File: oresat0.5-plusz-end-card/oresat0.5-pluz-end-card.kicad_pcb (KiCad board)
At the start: 4 copper layers, 99.8 x 94.6 mm, 45 parts, among them J1 J-SAMTEC-TFM-120-01-L-D-RA, J2 Harwin M55-7101242R, J3 Harwin M55-7101242R, J4 Harwin M55-7101242R, J5 Harwin M55-7101242R, J6 Conn_Coaxial

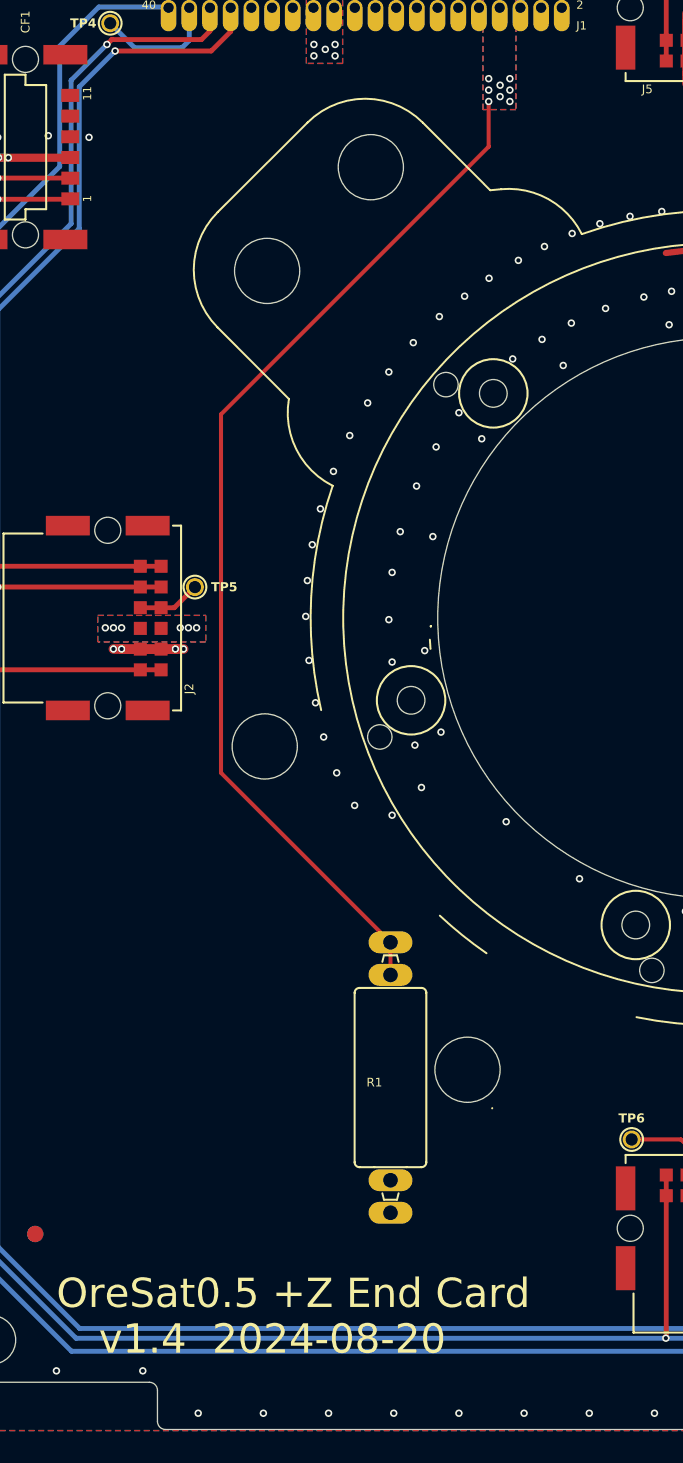
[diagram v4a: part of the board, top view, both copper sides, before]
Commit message: fixed silkscreen, fixed resistor helical deployer zone
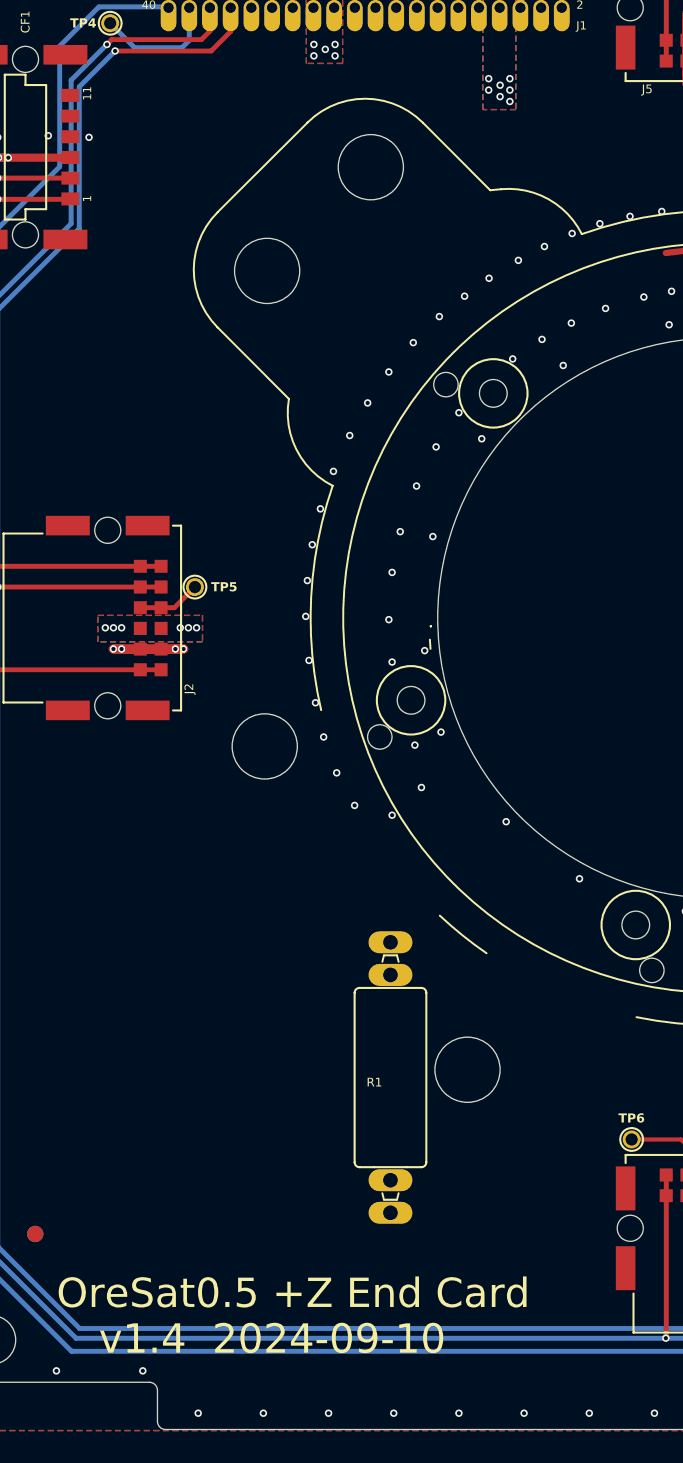
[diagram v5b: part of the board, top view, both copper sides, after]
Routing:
- net /HELICAL-DEPLOY: track 64.7 -> 0.00 mm, vias 8 -> 7
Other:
- board text added: "v1.4 2024-09-10"
- board text removed: "v1.4 2024-08-20"
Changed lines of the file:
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@@
 		(layer "F.SilkS")
 	)
-	(gr_line
-		(start 134.646944 132.575792)
-		(end 134.639949 132.592268)
-		(stroke
-			(width 0.12)
-			(type solid)
-		)
-		(layer "F.SilkS")
-	)
 	(gr_arc
 		(start 123.315615 72.08862)
@@
 		(layer "F.Fab")
 	)
-	(gr_text "v1.4  2024-08-20"
+	(gr_text "v1.4  2024-09-10"
 		(at 110.5 147.8 0)
 		(layer "F.SilkS")
@@
 		(net 4)
 	)
-	(segment
-		(start 118 90)
-		(end 134.4273 73.5727)
-		(width 0.25)
-		(layer "F.Cu")
-		(net 9)
-	)
-	(segment
-		(start 134.4273 73.5727)
-		(end 134.4273 70.8)
-		(width 0.25)
-		(layer "F.Cu")
-		(net 9)
-	)
-	(segment
-		(start 118 112)
-		(end 118 90)
-		(width 0.25)
-		(layer "F.Cu")
-		(net 9)
-	)
-	(segment
-		(start 128.400001 124.399999)
-		(end 128.400001 122.400001)
-		(width 0.25)
-		(layer "F.Cu")
-		(net 9)
-	)
-	(segment
-		(start 128.400001 122.400001)
-		(end 128.4 122.4)
-		(width 0.25)
-		(layer "F.Cu")
-		(net 9)
-	)
-	(segment
-		(start 128.4 122.4)
-		(end 118 112)
-		(width 0.25)
-		(layer "F.Cu")
-		(net 9)
-	)
 	(via
 		(at 135.7273 70.1)
@@
 		(net 9)
 	)
-	(via
-		(at 134.4273 70.8)
-		(size 0.4572)
-		(drill 0.254)
-		(layers "F.Cu" "B.Cu")
-		(free yes)
-		(net 9)
-	)
 	(segment
 		(start 120.8 59.9)
@@
 		(polygon
 			(pts
-				(xy 117.0635 103.9635) (xy 110.4365 103.9635) (xy 110.4365 102.3365) (xy 117.0635 102.3365)
+				(xy 116.8635 103.9635) (xy 110.4365 103.9635) (xy 110.4365 102.3365) (xy 116.8635 102.3365)
 			)
 		)
@@
 		(polygon
 			(pts
-				(xy 136.5 76.2) (xy 122 90.7) (xy 122 113.4) (xy 133.1 124.5) (xy 133.1 127.6) (xy 128.2 127.6)
-				(xy 128.2 124.596094) (xy 118 115) (xy 118 90) (xy 133.5 75) (xy 133.5 69.1) (xy 136.5 69.1)
+				(xy 136.5 76.2) (xy 122 90.7) (xy 122 108.4) (xy 120.140624 111.540624) (xy 130.6 122) (xy 130.6 126.1)
+				(xy 125.3 126.1) (xy 125.3 122.607522) (xy 113.515619 111.330111) (xy 117.6 106.086469) (xy 117.6 90.387096)
+				(xy 133.5 75) (xy 133.5 69.1) (xy 136.5 69.1)
 			)
 		)
@@
 			(pts
 				(xy 125.5635 65.8365) (xy 148.6635 65.8365) (xy 148.6635 68.4635) (xy 109.626302 68.4635) (xy 104.6635 73.426302)
-				(xy 104.6635 101.6365) (xy 117.0635 101.6365) (xy 117.0635 104.4635) (xy 104.6635 104.4635) (xy 104.6635 117.673698)
+				(xy 104.6635 101.6365) (xy 116.8635 101.6365) (xy 116.8635 104.4635) (xy 104.6635 104.4635) (xy 104.6635 117.673698)
 				(xy 130.326302 143.3365) (xy 147.5365 143.3365) (xy 147.5365 133.9365) (xy 150.6635 133.9365) (xy 150.6635 143.3365)
 				(xy 157.573585 143.3365) (xy 181.1365 119.800226) (xy 181.1365 101.0365) (xy 185.2635 101.0365)

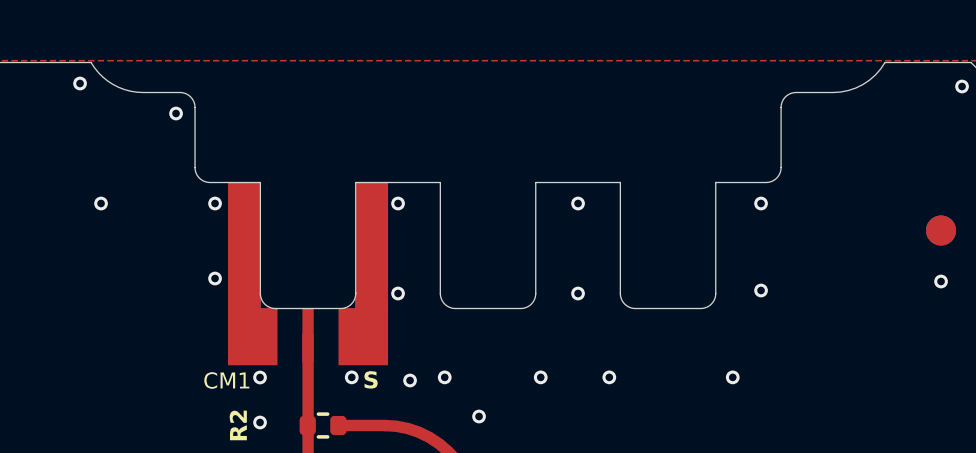
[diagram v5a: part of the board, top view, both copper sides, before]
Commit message: added components in symbol field for BOM
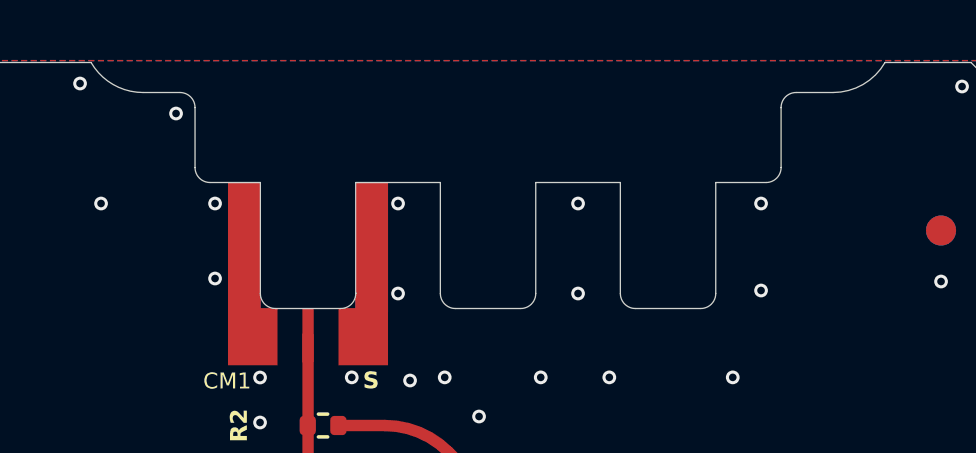
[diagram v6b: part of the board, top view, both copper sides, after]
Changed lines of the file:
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@@
 		(fp_arc
 			(start 17.73205 -43.8)
-			(mid 18.085606 -43.653542)
+			(mid 18.085571 -43.653536)
 			(end 18.23205 -43.3)
 			(stroke
@@
 		(fp_arc
 			(start 18.73205 -40.8)
-			(mid 18.378494 -40.946458)
+			(mid 18.378529 -40.946464)
 			(end 18.23205 -41.3)
 			(stroke
@@
 		(fp_arc
 			(start 37.76795 -43.3)
-			(mid 37.9144 -43.653536)
+			(mid 37.914394 -43.653571)
 			(end 38.26795 -43.8)
 			(stroke
@@
 		(fp_arc
 			(start 37.76795 -41.3)
-			(mid 37.6215 -40.946464)
+			(mid 37.621506 -40.946429)
 			(end 37.26795 -40.8)
 			(stroke
@@
 		(fp_arc
 			(start 17.73205 -43.8)
-			(mid 18.085606 -43.653542)
+			(mid 18.085571 -43.653536)
 			(end 18.23205 -43.3)
 			(stroke
@@
 		(fp_arc
 			(start 18.73205 -40.8)
-			(mid 18.378494 -40.946458)
+			(mid 18.378529 -40.946464)
 			(end 18.23205 -41.3)
 			(stroke
@@
 		(fp_arc
 			(start 37.76795 -43.3)
-			(mid 37.9144 -43.653536)
+			(mid 37.914394 -43.653571)
 			(end 38.26795 -43.8)
 			(stroke
@@
 		(fp_arc
 			(start 37.76795 -41.3)
-			(mid 37.6215 -40.946464)
+			(mid 37.621506 -40.946429)
 			(end 37.26795 -40.8)
 			(stroke

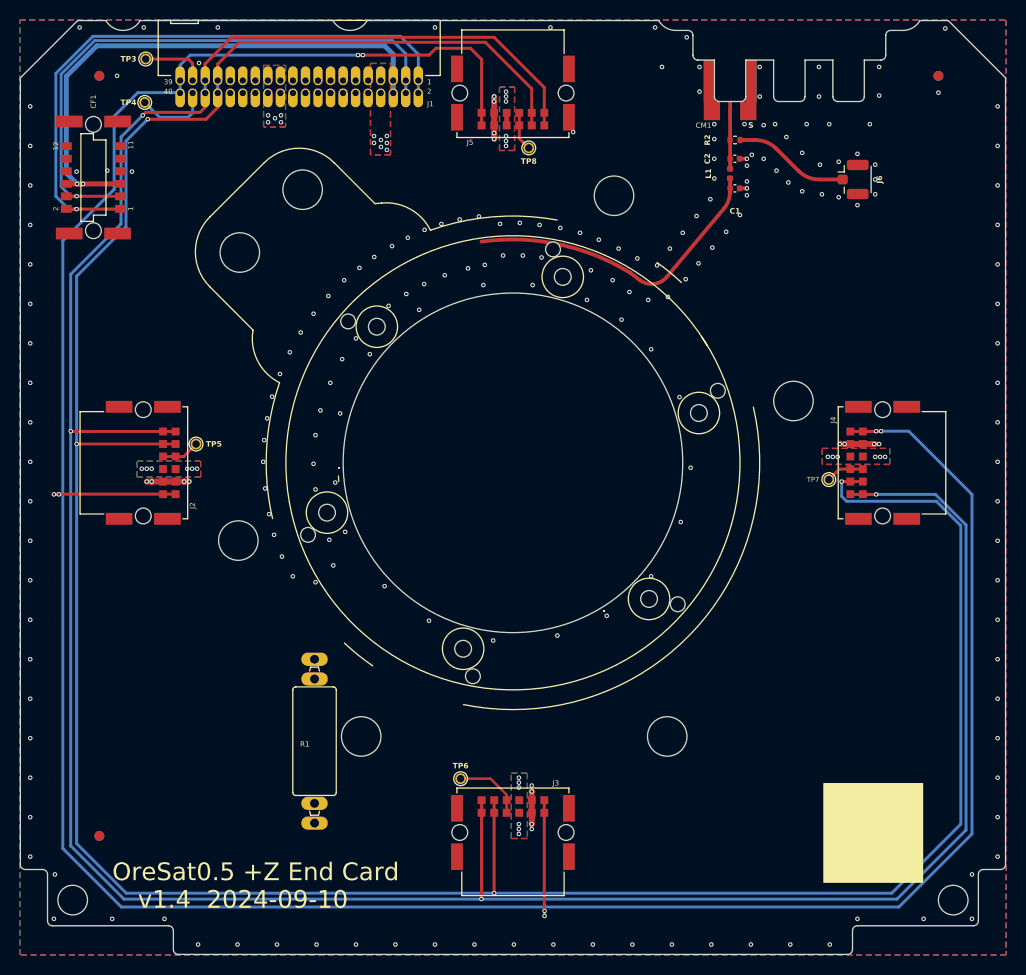
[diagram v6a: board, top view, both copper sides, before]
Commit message: Final polish for v1.4. Added more stiching vias, cleaned up some DRCs that were stupid, added more layers to deployment resistor pads, now  sending off to Osh Park.
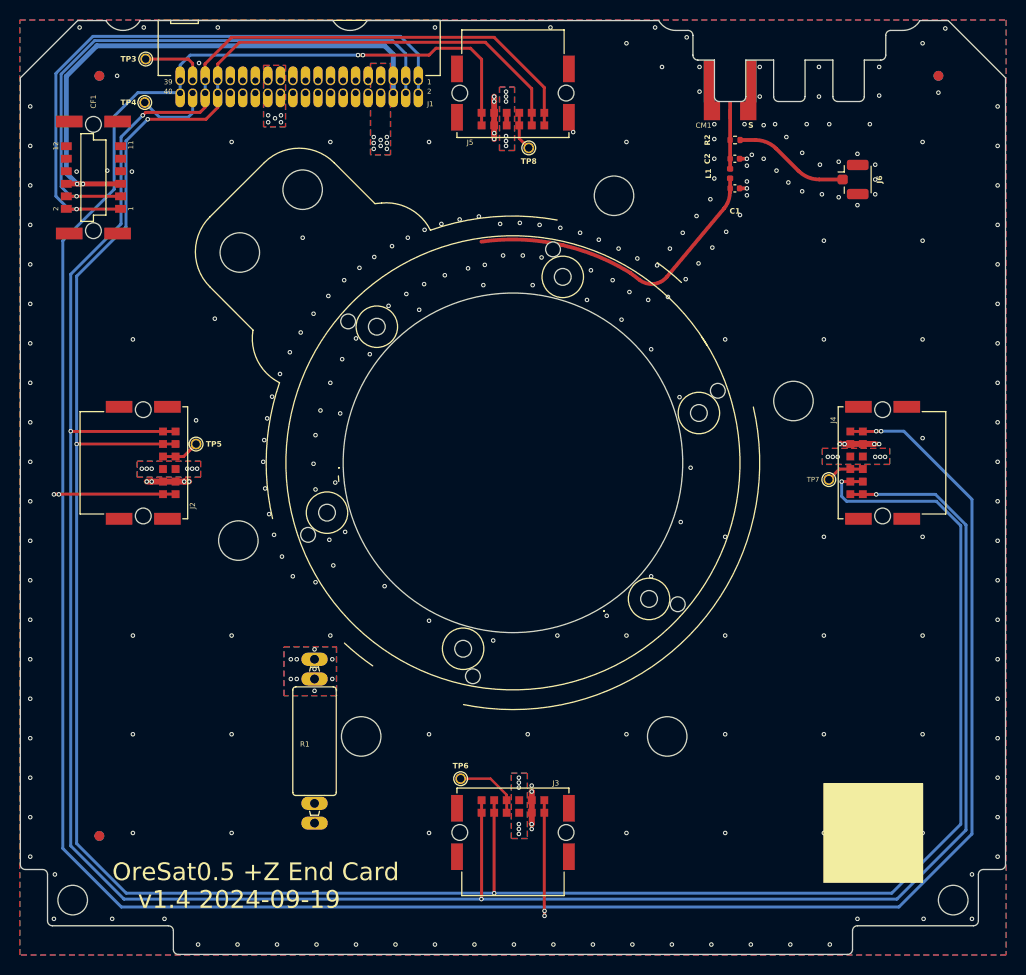
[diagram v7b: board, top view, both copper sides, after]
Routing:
- net GND: vias 220 -> 262
- net /HELICAL-DEPLOY: vias 7 -> 17
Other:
- board text added: "v${REVISION} ${ISSUE_DATE}"
- board text removed: "v1.4 2024-09-10"
